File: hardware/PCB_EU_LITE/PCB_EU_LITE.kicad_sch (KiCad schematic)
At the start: 0 parts

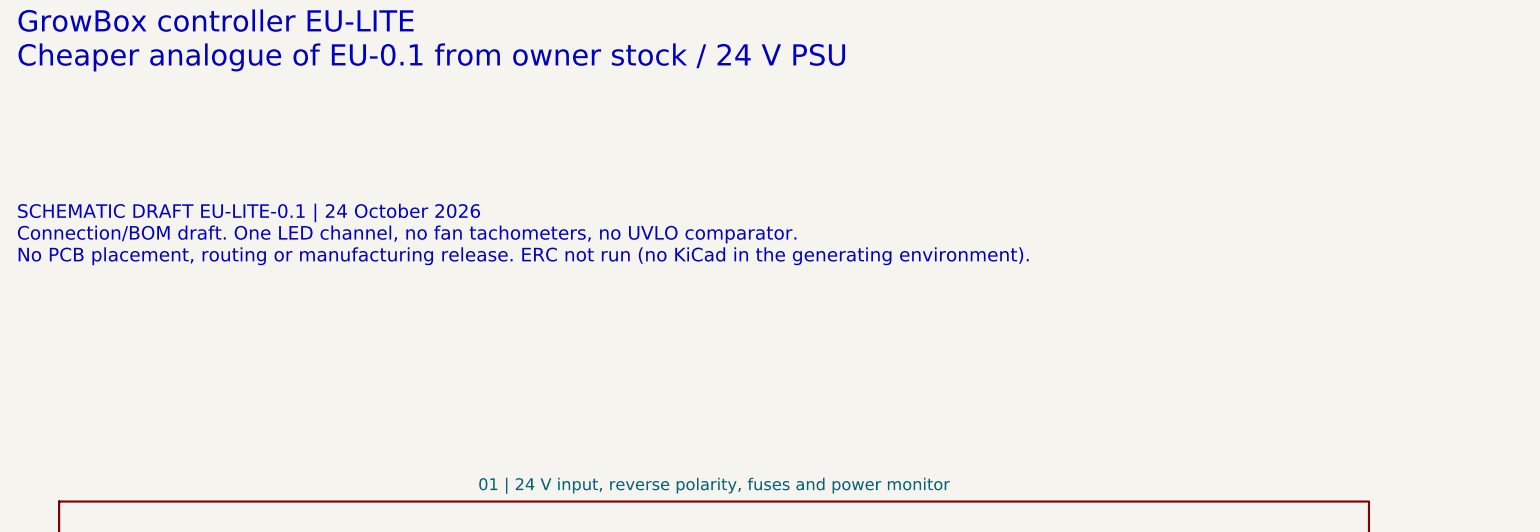
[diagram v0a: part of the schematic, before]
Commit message: Place EU-LITE components on top with the battery underneath
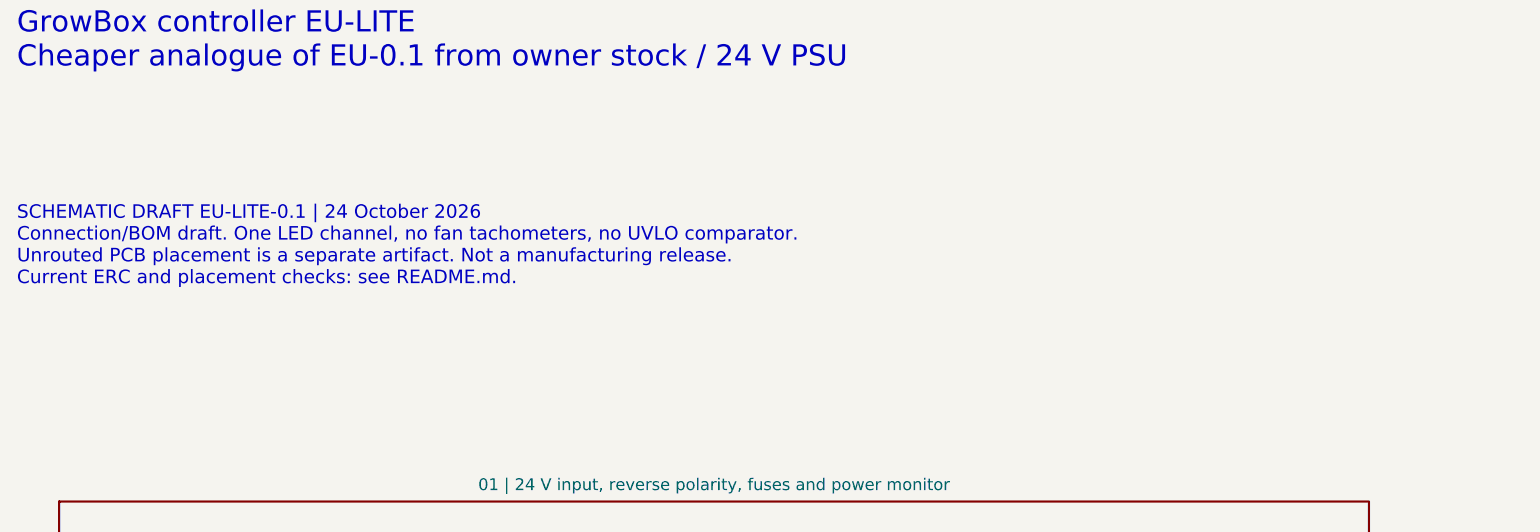
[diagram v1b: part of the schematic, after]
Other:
- note added: "SCHEMATIC DRAFT EU-LITE-0.1 | 24 October 2026 Connection/BOM draft. One LED channel, no fan tachometers, no UVLO comparator. Unrouted PCB placement is a separate artifact. Not a manufacturing release. Current ERC and placement checks: see README.md."
- note removed: "SCHEMATIC DRAFT EU-LITE-0.1 | 24 October 2026 Connection/BOM draft. One LED channel, no fan tachometers, no UVLO comparator. No PCB placement, routing or manufacturing release. ERC not run (no KiCad in the generating environment)."
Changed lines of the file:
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@@
 (kicad_sch (version 20260306) (generator "eeschema") (generator_version "10.0") (paper "A3") (title_block (title "GrowBox | EU-LITE | schematic review") (date "2026-10-24") (rev "EU-LITE-0.1") (company "GrowBox | EU-LITE from stock") (comment 1 "SCHEMATIC DRAFT | no PCB / manufacturing release"))
 (text "GrowBox controller EU-LITE\nCheaper analogue of EU-0.1 from owner stock / 24 V PSU" (at 20 17 0) (effects (font (size 2.5 2.5)) (justify left top)))
-(text "SCHEMATIC DRAFT EU-LITE-0.1 | 24 October 2026\nConnection/BOM draft. One LED channel, no fan tachometers, no UVLO comparator.\nNo PCB placement, routing or manufacturing release. ERC not run (no KiCad in the generating environment)." (at 20 40 0) (effects (font (size 1.6 1.6)) (justify left top)))
+(text "SCHEMATIC DRAFT EU-LITE-0.1 | 24 October 2026\nConnection/BOM draft. One LED channel, no fan tachometers, no UVLO comparator.\nUnrouted PCB placement is a separate artifact. Not a manufacturing release.\nCurrent ERC and placement checks: see README.md." (at 20 40 0) (effects (font (size 1.6 1.6)) (justify left top)))
 (sheet (at 25 75) (size 155 28) (stroke (width 0.254) (type default)) (fill (color 0 0 0 0)) (property "Sheetname" "01 | 24 V input, reverse polarity, fuses and power monitor" (at 102.5 73 0) (effects (font (size 1.4 1.4)) )) (property "Sheetfile" "InputPower.kicad_sch" (at 102.5 105 0) (effects (font (size 1 1)) )) (instances (project "PCB_EU_LITE" (path "/6650c329-4f4f-5b7a-a019-ee8e8f2772e1" (page "2")))))
 (sheet (at 210 75) (size 155 28) (stroke (width 0.254) (type default)) (fill (color 0 0 0 0)) (property "Sheetname" "02 | 24 V to 12 V buck (ST1S14)" (at 287.5 73 0) (effects (font (size 1.4 1.4)) )) (property "Sheetfile" "Aux12V.kicad_sch" (at 287.5 105 0) (effects (font (size 1 1)) )) (instances (project "PCB_EU_LITE" (path "/6650c329-4f4f-5b7a-a019-ee8e8f2772e1" (page "3")))))

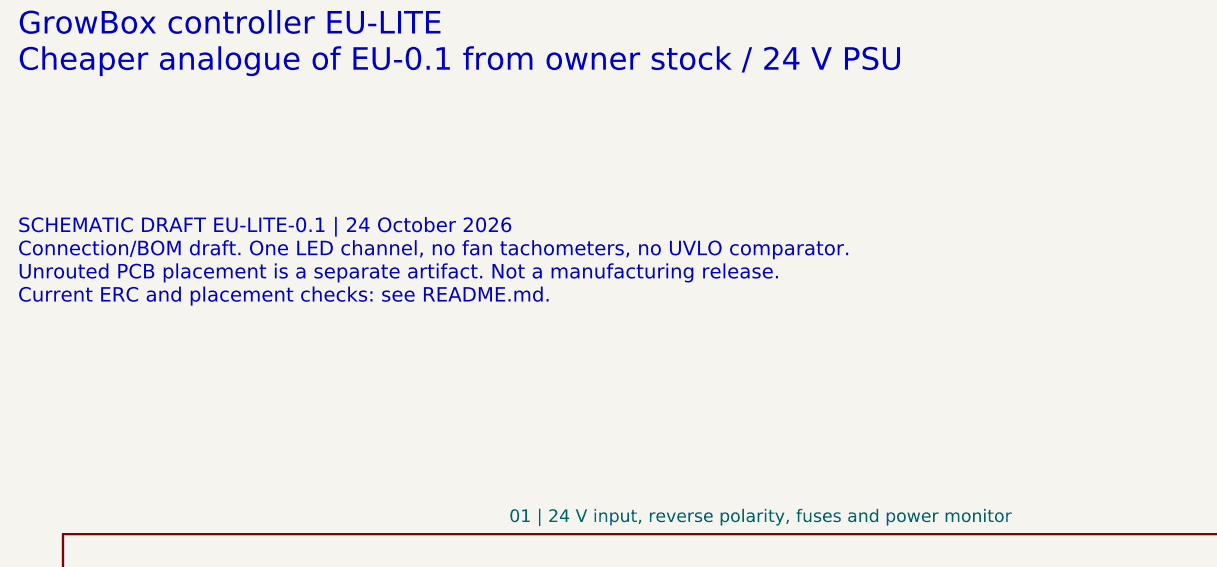
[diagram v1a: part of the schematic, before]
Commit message: Finish EU-LITE LED routing and parallel outputs
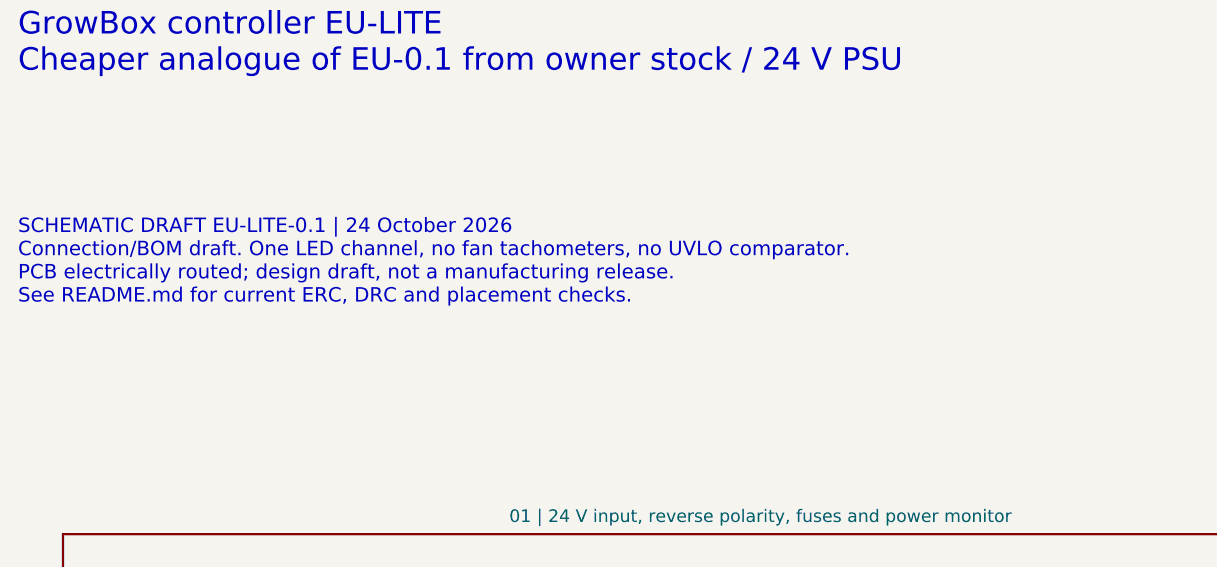
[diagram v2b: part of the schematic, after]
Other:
- note added: "SCHEMATIC DRAFT EU-LITE-0.1 | 24 October 2026 Connection/BOM draft. One LED channel, no fan tachometers, no UVLO comparator. PCB electrically routed; design draft, not a manufacturing release. See README.md for current ERC, DRC and placement checks."
- note removed: "SCHEMATIC DRAFT EU-LITE-0.1 | 24 October 2026 Connection/BOM draft. One LED channel, no fan tachometers, no UVLO comparator. Unrouted PCB placement is a separate artifact. Not a manufacturing release. Current ERC and placement checks: see README.md."
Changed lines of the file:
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@@
 (kicad_sch (version 20260306) (generator "eeschema") (generator_version "10.0") (paper "A3") (title_block (title "GrowBox | EU-LITE | schematic review") (date "2026-10-24") (rev "EU-LITE-0.1") (company "GrowBox | EU-LITE from stock") (comment 1 "SCHEMATIC DRAFT | no PCB / manufacturing release"))
 (text "GrowBox controller EU-LITE\nCheaper analogue of EU-0.1 from owner stock / 24 V PSU" (at 20 17 0) (effects (font (size 2.5 2.5)) (justify left top)))
-(text "SCHEMATIC DRAFT EU-LITE-0.1 | 24 October 2026\nConnection/BOM draft. One LED channel, no fan tachometers, no UVLO comparator.\nUnrouted PCB placement is a separate artifact. Not a manufacturing release.\nCurrent ERC and placement checks: see README.md." (at 20 40 0) (effects (font (size 1.6 1.6)) (justify left top)))
+(text "SCHEMATIC DRAFT EU-LITE-0.1 | 24 October 2026\nConnection/BOM draft. One LED channel, no fan tachometers, no UVLO comparator.\nPCB electrically routed; design draft, not a manufacturing release.\nSee README.md for current ERC, DRC and placement checks." (at 20 40 0) (effects (font (size 1.6 1.6)) (justify left top)))
 (sheet (at 25 75) (size 155 28) (stroke (width 0.254) (type default)) (fill (color 0 0 0 0)) (property "Sheetname" "01 | 24 V input, reverse polarity, fuses and power monitor" (at 102.5 73 0) (effects (font (size 1.4 1.4)) )) (property "Sheetfile" "InputPower.kicad_sch" (at 102.5 105 0) (effects (font (size 1 1)) )) (instances (project "PCB_EU_LITE" (path "/6650c329-4f4f-5b7a-a019-ee8e8f2772e1" (page "2")))))
 (sheet (at 210 75) (size 155 28) (stroke (width 0.254) (type default)) (fill (color 0 0 0 0)) (property "Sheetname" "02 | 24 V to 12 V buck (ST1S14)" (at 287.5 73 0) (effects (font (size 1.4 1.4)) )) (property "Sheetfile" "Aux12V.kicad_sch" (at 287.5 105 0) (effects (font (size 1 1)) )) (instances (project "PCB_EU_LITE" (path "/6650c329-4f4f-5b7a-a019-ee8e8f2772e1" (page "3")))))
